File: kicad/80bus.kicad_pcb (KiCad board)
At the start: 2 copper layers, 157 x 203.2 mm, 11 parts, among them J1 Conn_01x80, J2 Conn_01x80, J3 Conn_01x80, J4 Conn_01x80, J5 Conn_01x80, J6 Conn_01x80, SW1 Reset, T1 Terminal_01x05

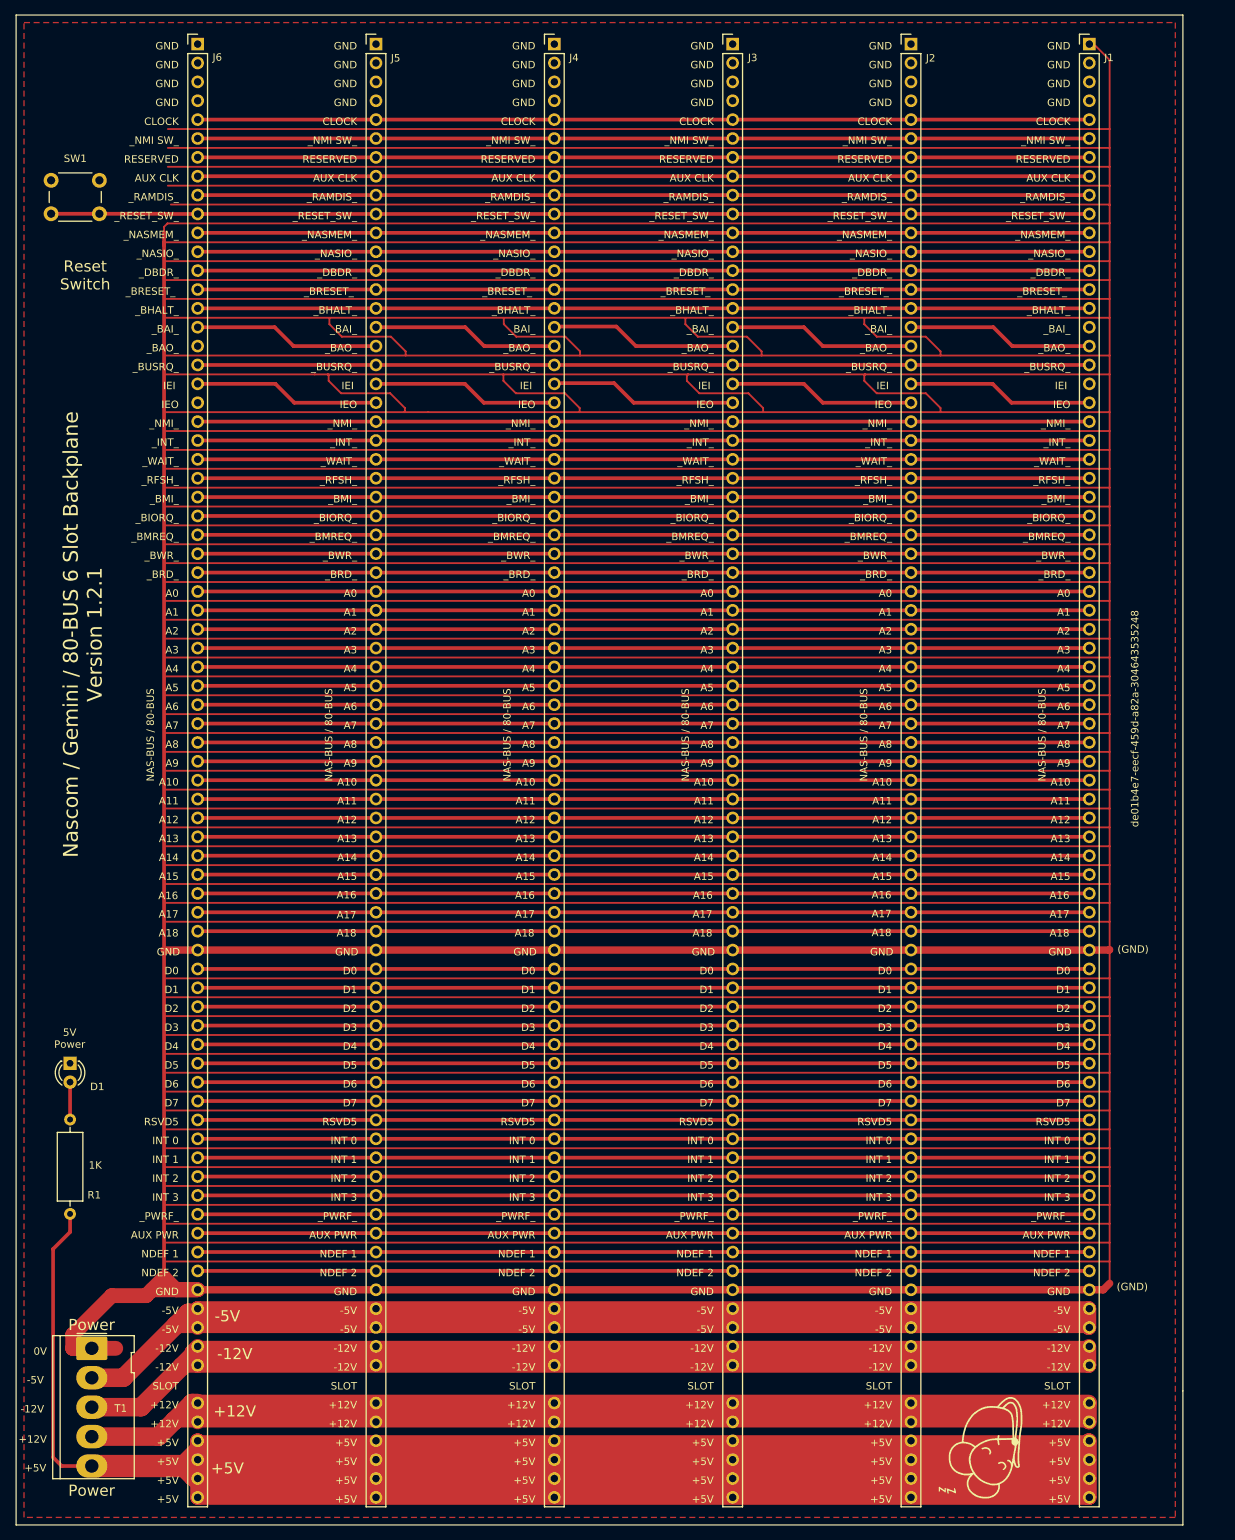
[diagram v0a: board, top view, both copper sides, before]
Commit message: Add mounting holes
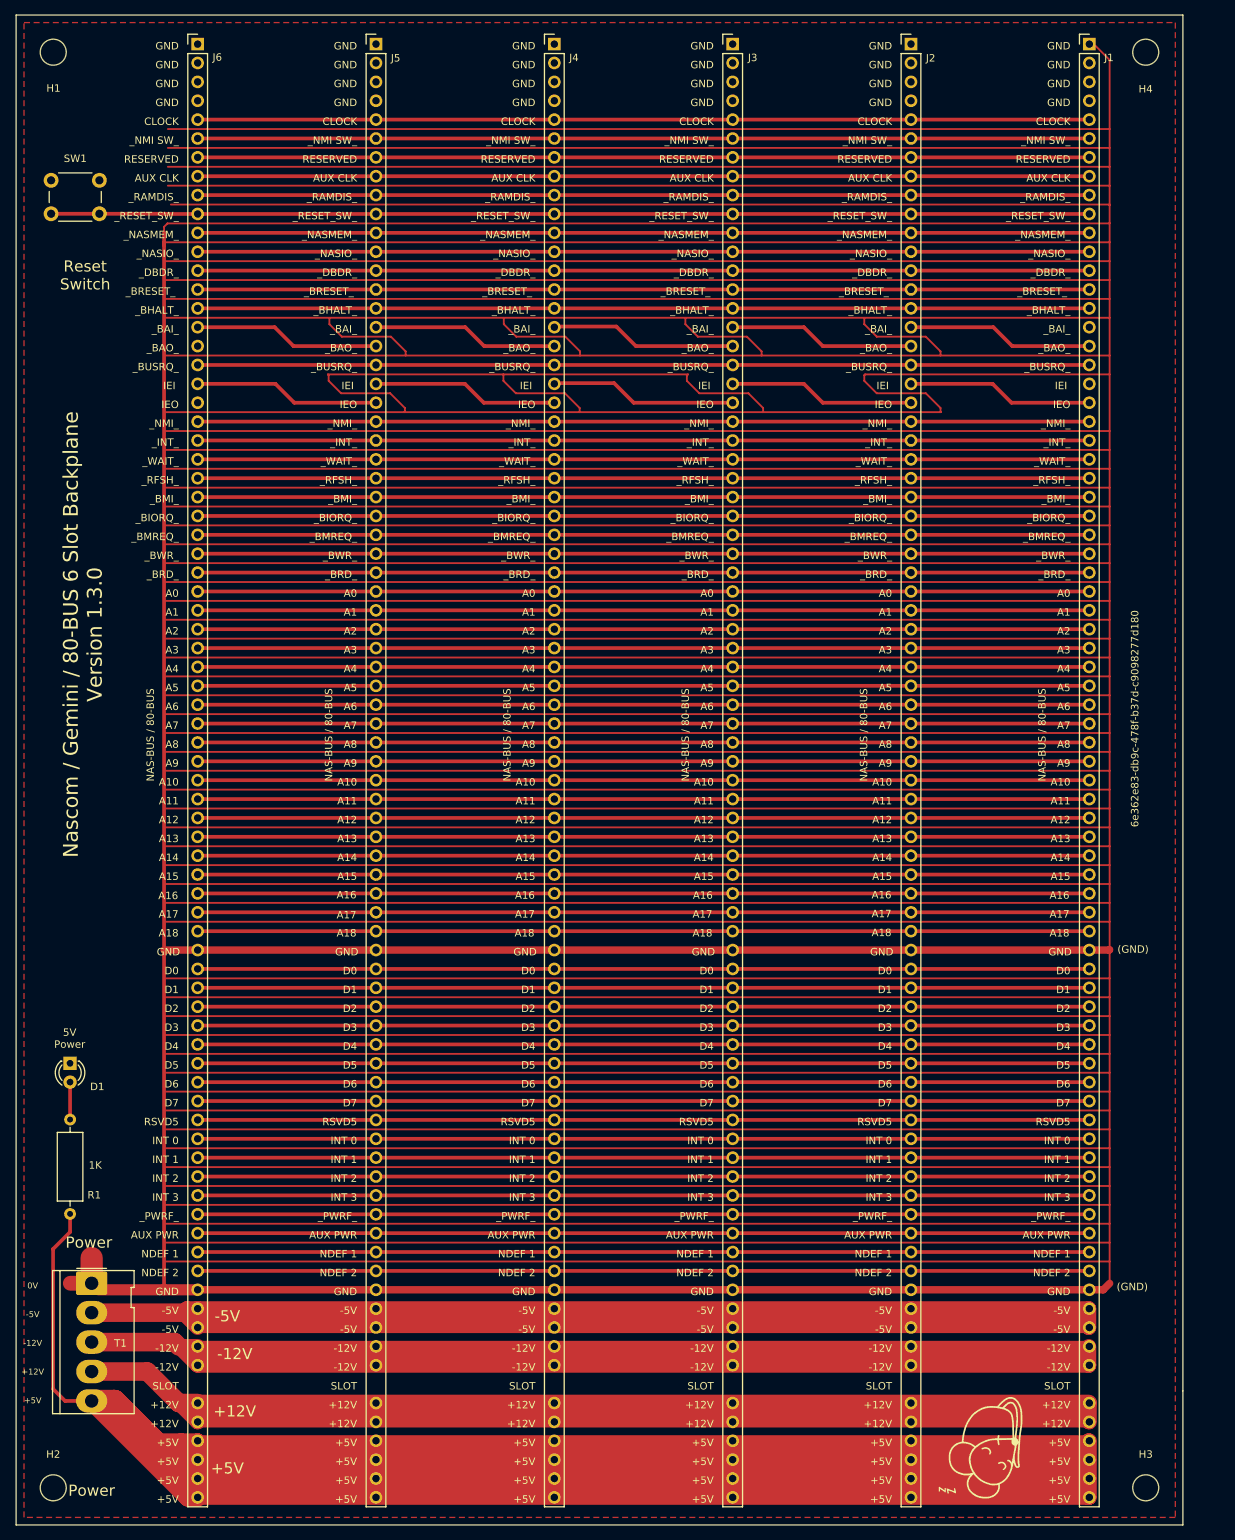
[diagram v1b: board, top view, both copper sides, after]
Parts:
- added H1: MountingHole, MountingHole:MountingHole_3.5mm, F.Cu at (106.8, 50.3)
- added H2: MountingHole, MountingHole:MountingHole_3.5mm, F.Cu at (106.8, 243.5)
- added H3: MountingHole, MountingHole:MountingHole_3.5mm, F.Cu at (253.8, 243.5)
- added H4: MountingHole, MountingHole:MountingHole_3.5mm, F.Cu at (253.8, 50.3)
- moved T1 8.76 mm to (112.0, 216.0)
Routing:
- net GND: track 7951.5 -> 7869.0 mm
- net +5V: track 924.1 -> 974.5 mm
- net +12V: track 385.2 -> 391.5 mm
- net -5V: track 388.5 -> 382.4 mm
- net -12V: track 385.4 -> 381.7 mm
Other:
- board text added: "0V -5V -12V +12V +5V"
- board text added: "6e362e83-db9c-478f-b37d-c9098277d180"
- board text added: "Nascom / Gemini / 80-BUS 6 Slot Backplane Version 1.3.0"
- board text removed: "0V"
- board text removed: "Nascom / Gemini / 80-BUS 6 Slot Backplane Version 1.2.1"
- board text removed: "de01b4e7-eecf-459d-a82a-304643535248"

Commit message: Kicad, enhanced power, moved mount holes
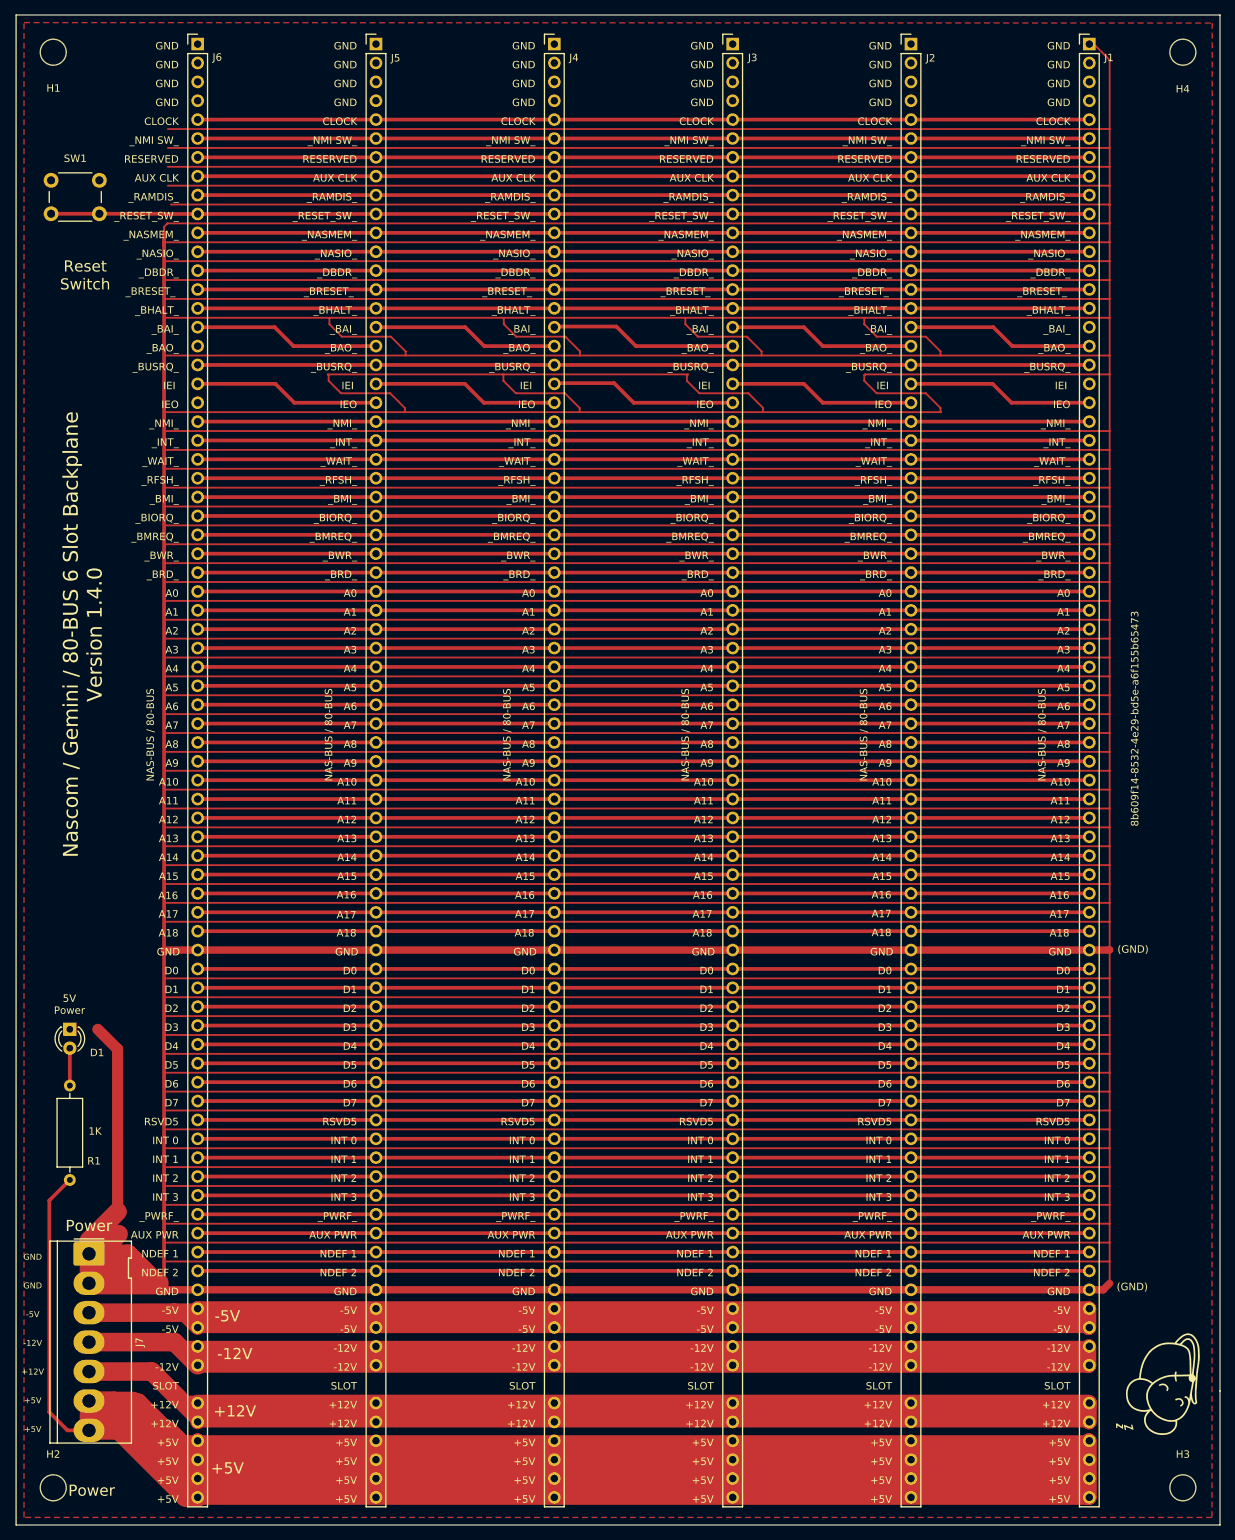
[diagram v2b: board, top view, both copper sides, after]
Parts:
- removed T1: Terminal_01x05, Connector_Molex:Molex_KK-396_5273-05A_1x05_P3.96mm_Vertical
- added J7: Screw_Terminal_01x07, Connector_Molex:Molex_KK-396_5273-07A_1x07_P3.96mm_Vertical, F.Cu at (111.6, 212.0)
- moved G1 25.3 mm to (255.9, 230.0)
- moved H3 5.00 mm to (258.8, 243.5)
- moved H4 5.00 mm to (258.8, 50.3)
- moved D1 4.57 mm to (109.1, 181.8)
- moved R1 4.57 mm to (109.1, 202.1)
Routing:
- net GND: track 7869.0 -> 7930.0 mm
- net +5V: track 974.5 -> 1011.7 mm
- net -5V: track 382.4 -> 383.8 mm
- net +12V: track 391.5 -> 391.0 mm
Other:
- board size 157 x 203.2 mm -> 162 x 203.2 mm
- board text added: "8b609f14-8532-4e29-bd5e-a6f155b65473"
- board text added: "GND GND -5V -12V +12V +5V +5V"
- board text added: "Nascom / Gemini / 80-BUS 6 Slot Backplane Version 1.4.0"
- board text removed: "0V -5V -12V +12V +5V"
- board text removed: "6e362e83-db9c-478f-b37d-c9098277d180"
- board text removed: "Nascom / Gemini / 80-BUS 6 Slot Backplane Version 1.3.0"

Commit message: Kicad 9 and Docs
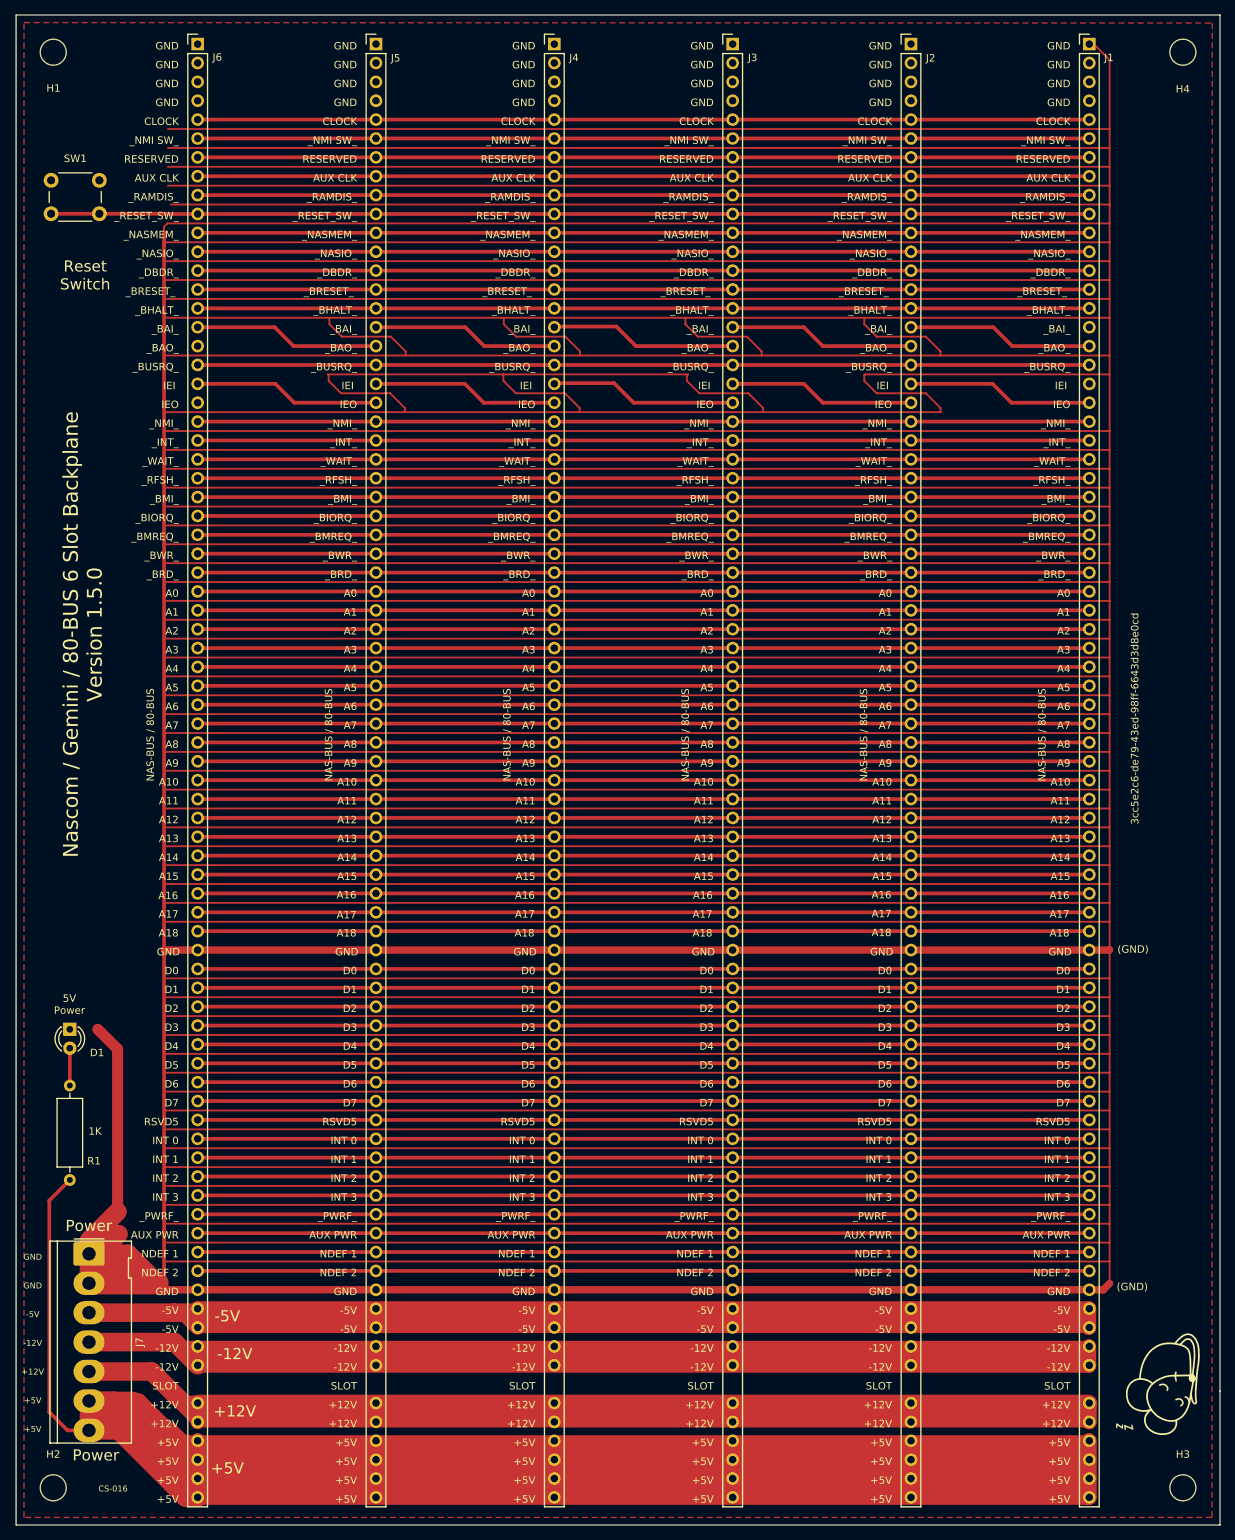
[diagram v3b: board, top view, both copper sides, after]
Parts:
- added G001: LOGO, 80bus:qr code, B.Cu at (113.5, 146.0)
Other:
- board text added: "3cc5e2c6-de79-43ed-98ff-6643d3d8e0cd"
- board text added: "CS-016"
- board text added: "Documentation -->"
- board text added: "Nascom / Gemini / 80-BUS 6 Slot Backplane Version 1.5.0"
- board text removed: "8b609f14-8532-4e29-bd5e-a6f155b65473"
- board text removed: "Nascom / Gemini / 80-BUS 6 Slot Backplane Version 1.4.0"
